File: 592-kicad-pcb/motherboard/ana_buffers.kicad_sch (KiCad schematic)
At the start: 9 parts, among them J2 U.FL, J3 U.FL, U4 OPA2328DR, U5 74LVC1T45GW

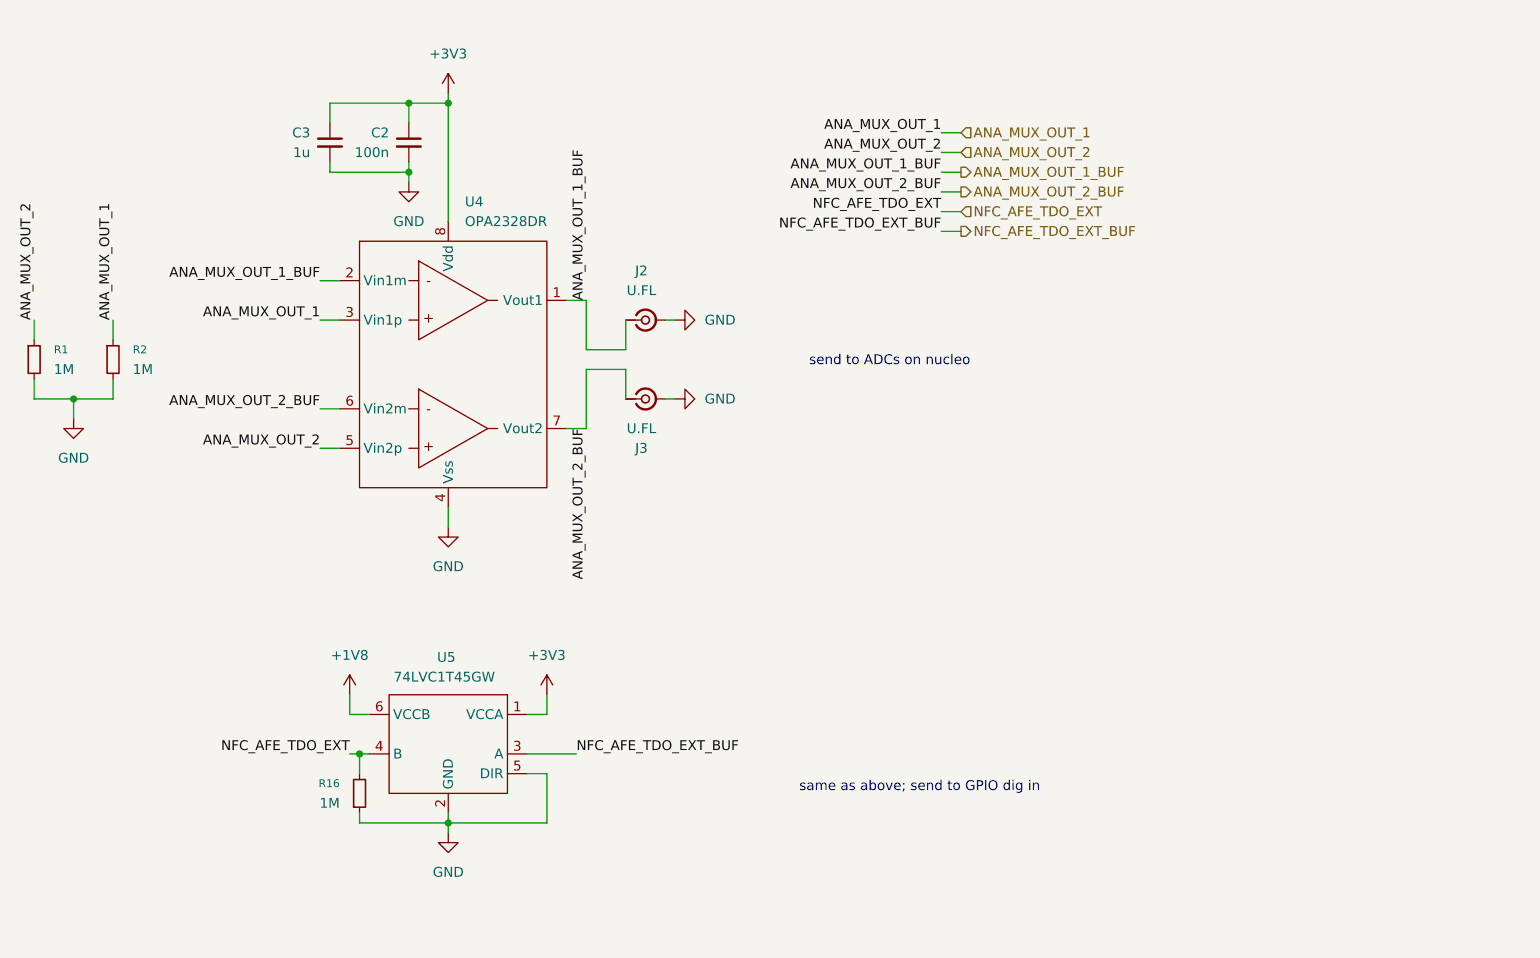
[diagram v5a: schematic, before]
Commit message: clean up schematics, add proper connectors
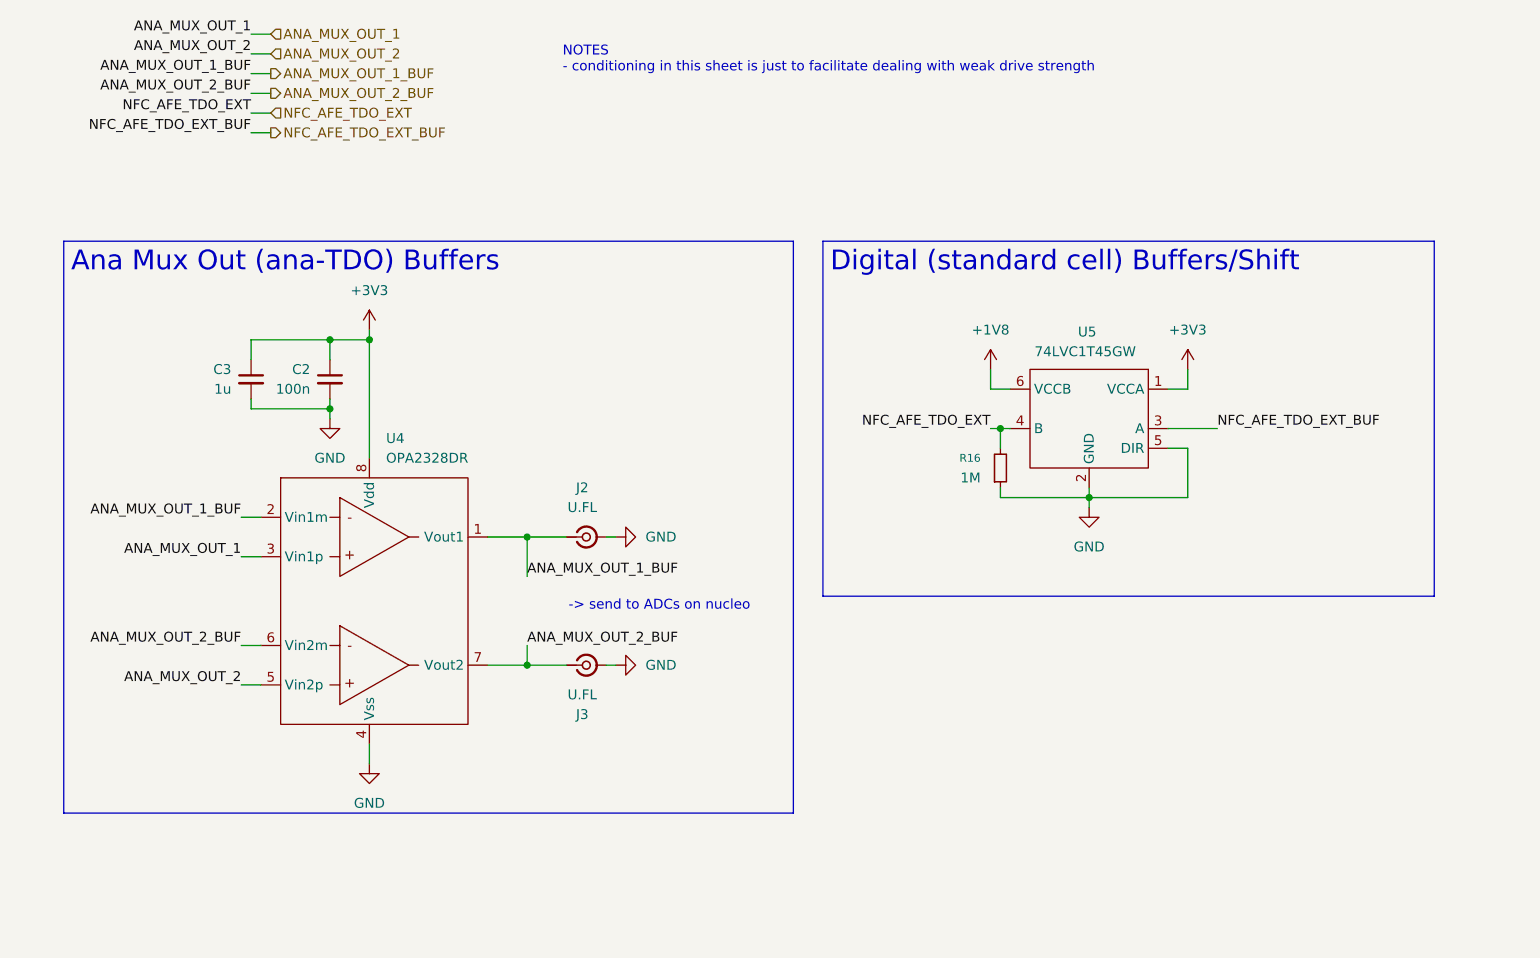
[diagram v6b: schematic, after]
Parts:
- removed R1, R2: 1M, Resistor_SMD:R_0603_1608Metric, symbol Device:R_Small
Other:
- note added: "-> send to ADCs on nucleo"
- note added: "NOTES - conditioning in this sheet is just to facilitate dealing with weak drive strength"
- note removed: "same as above; send to GPIO dig in"
- note removed: "send to ADCs on nucleo"
- moved on the sheet: C2, C3, J2, J3, R16, U4, U5

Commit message: combine hierarchy of all sans power
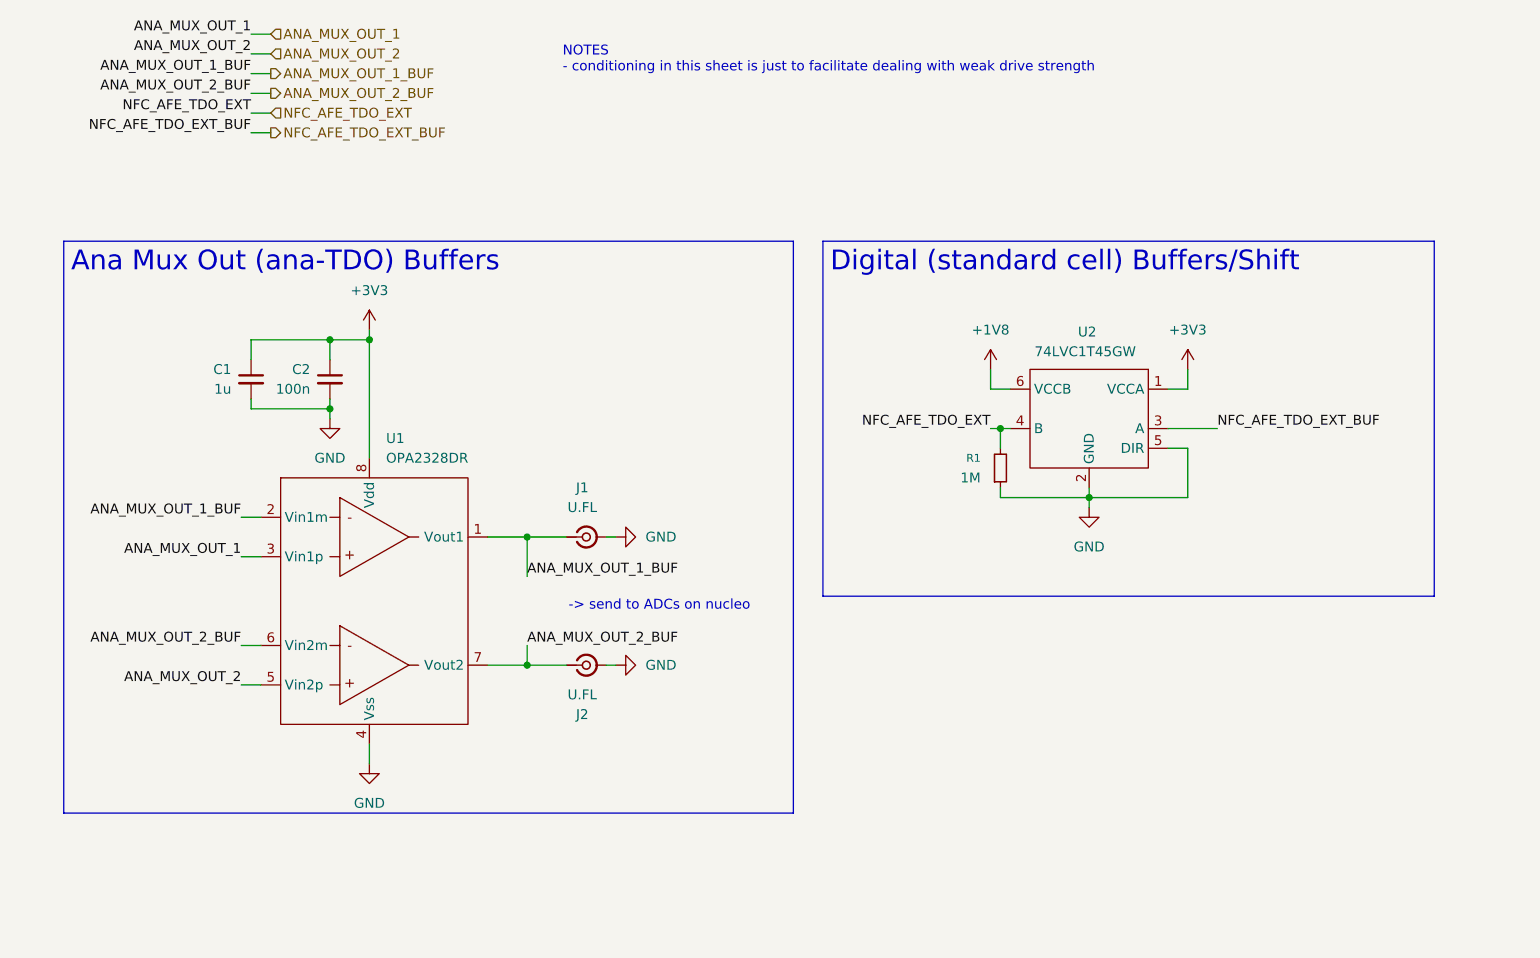
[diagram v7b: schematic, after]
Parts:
- renumbered C3 to C1, J2 to J1, J3 to J2, R16 to R1, U4 to U1, U5 to U2
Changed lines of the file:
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@@
 		(dnp no)
 		(fields_autoplaced yes)
-		(property "Reference" "#PWR019"
+		(property "Reference" "#PWR05"
 			(at 97.79 102.87 0)
 			(effects
@@
 		(instances
 			(project "motherboard"
-				(path "/5b0c97ac-fa03-4db8-b41b-0eee32b6f55d/9cc7bda2-6b63-4506-9986-d8a2a58c5915"
-					(reference "#PWR019")
+				(path "/5b0c97ac-fa03-4db8-b41b-0eee32b6f55d/f049e4ad-bebe-4338-850a-2727de737ae9/cc4799d4-5517-451a-9b97-5b1497b0c7e9"
+					(reference "#PWR05")
 					(unit 1)
 				)
@@
 		(dnp no)
 		(fields_autoplaced yes)
-		(property "Reference" "J2"
+		(property "Reference" "J1"
 			(at 87.1104 80.01 0)
 			(effects
@@
 		)
 		(instances
-			(project ""
-				(path "/5b0c97ac-fa03-4db8-b41b-0eee32b6f55d/9cc7bda2-6b63-4506-9986-d8a2a58c5915"
-					(reference "J2")
+			(project "motherboard"
+				(path "/5b0c97ac-fa03-4db8-b41b-0eee32b6f55d/f049e4ad-bebe-4338-850a-2727de737ae9/cc4799d4-5517-451a-9b97-5b1497b0c7e9"
+					(reference "J1")
 					(unit 1)
 				)
@@
 		(dnp no)
 		(fields_autoplaced yes)
-		(property "Reference" "#PWR013"
+		(property "Reference" "#PWR02"
 			(at 59.69 63.5 0)
 			(effects
@@
 		)
 		(instances
-			(project ""
-				(path "/5b0c97ac-fa03-4db8-b41b-0eee32b6f55d/9cc7bda2-6b63-4506-9986-d8a2a58c5915"
-					(reference "#PWR013")
+			(project "motherboard"
+				(path "/5b0c97ac-fa03-4db8-b41b-0eee32b6f55d/f049e4ad-bebe-4338-850a-2727de737ae9/cc4799d4-5517-451a-9b97-5b1497b0c7e9"
+					(reference "#PWR02")
 					(unit 1)
 				)
@@
 		(dnp no)
 		(fields_autoplaced yes)
-		(property "Reference" "#PWR020"
+		(property "Reference" "#PWR07"
 			(at 152.4 88.9 0)
 			(effects
@@
 		(instances
 			(project "motherboard"
-				(path "/5b0c97ac-fa03-4db8-b41b-0eee32b6f55d/9cc7bda2-6b63-4506-9986-d8a2a58c5915"
-					(reference "#PWR020")
+				(path "/5b0c97ac-fa03-4db8-b41b-0eee32b6f55d/f049e4ad-bebe-4338-850a-2727de737ae9/cc4799d4-5517-451a-9b97-5b1497b0c7e9"
+					(reference "#PWR07")
 					(unit 1)
 				)
@@
 		(dnp no)
 		(fields_autoplaced yes)
-		(property "Reference" "#PWR012"
+		(property "Reference" "#PWR03"
 			(at 59.69 121.92 0)
 			(effects
@@
 		)
 		(instances
-			(project ""
-				(path "/5b0c97ac-fa03-4db8-b41b-0eee32b6f55d/9cc7bda2-6b63-4506-9986-d8a2a58c5915"
-					(reference "#PWR012")
+			(project "motherboard"
+				(path "/5b0c97ac-fa03-4db8-b41b-0eee32b6f55d/f049e4ad-bebe-4338-850a-2727de737ae9/cc4799d4-5517-451a-9b97-5b1497b0c7e9"
+					(reference "#PWR03")
 					(unit 1)
 				)
@@
 		(on_board yes)
 		(dnp no)
-		(property "Reference" "U5"
+		(property "Reference" "U2"
 			(at 152.146 59.944 0)
 			(effects
@@
 		)
 		(instances
-			(project ""
-				(path "/5b0c97ac-fa03-4db8-b41b-0eee32b6f55d/9cc7bda2-6b63-4506-9986-d8a2a58c5915"
-					(reference "U5")
+			(project "motherboard"
+				(path "/5b0c97ac-fa03-4db8-b41b-0eee32b6f55d/f049e4ad-bebe-4338-850a-2727de737ae9/cc4799d4-5517-451a-9b97-5b1497b0c7e9"
+					(reference "U2")
 					(unit 1)
 				)
@@
 		(dnp no)
 		(fields_autoplaced yes)
-		(property "Reference" "#PWR022"
+		(property "Reference" "#PWR08"
 			(at 165.1 68.58 0)
 			(effects
@@
 		(instances
 			(project "motherboard"
-				(path "/5b0c97ac-fa03-4db8-b41b-0eee32b6f55d/9cc7bda2-6b63-4506-9986-d8a2a58c5915"
-					(reference "#PWR022")
+				(path "/5b0c97ac-fa03-4db8-b41b-0eee32b6f55d/f049e4ad-bebe-4338-850a-2727de737ae9/cc4799d4-5517-451a-9b97-5b1497b0c7e9"
+					(reference "#PWR08")
 					(unit 1)
 				)
@@
 		(dnp no)
 		(fields_autoplaced yes)
-		(property "Reference" "#PWR018"
+		(property "Reference" "#PWR04"
 			(at 97.79 86.36 0)
 			(effects
@@
 		(instances
 			(project "motherboard"
-				(path "/5b0c97ac-fa03-4db8-b41b-0eee32b6f55d/9cc7bda2-6b63-4506-9986-d8a2a58c5915"
-					(reference "#PWR018")
+				(path "/5b0c97ac-fa03-4db8-b41b-0eee32b6f55d/f049e4ad-bebe-4338-850a-2727de737ae9/cc4799d4-5517-451a-9b97-5b1497b0c7e9"
+					(reference "#PWR04")
 					(unit 1)
 				)
@@
 		(on_board yes)
 		(dnp no)
-		(property "Reference" "U4"
+		(property "Reference" "U1"
 			(at 61.8333 73.66 0)
 			(effects
@@
 		)
 		(instances
-			(project ""
-				(path "/5b0c97ac-fa03-4db8-b41b-0eee32b6f55d/9cc7bda2-6b63-4506-9986-d8a2a58c5915"
-					(reference "U4")
+			(project "motherboard"
+				(path "/5b0c97ac-fa03-4db8-b41b-0eee32b6f55d/f049e4ad-bebe-4338-850a-2727de737ae9/cc4799d4-5517-451a-9b97-5b1497b0c7e9"
+					(reference "U1")
 					(unit 1)
 				)
@@
 		(dnp no)
 		(fields_autoplaced yes)
-		(property "Reference" "#PWR014"
+		(property "Reference" "#PWR01"
 			(at 54.61 77.47 0)
 			(effects
@@
 		(instances
 			(project "motherboard"
-				(path "/5b0c97ac-fa03-4db8-b41b-0eee32b6f55d/9cc7bda2-6b63-4506-9986-d8a2a58c5915"
-					(reference "#PWR014")
+				(path "/5b0c97ac-fa03-4db8-b41b-0eee32b6f55d/f049e4ad-bebe-4338-850a-2727de737ae9/cc4799d4-5517-451a-9b97-5b1497b0c7e9"
+					(reference "#PWR01")
 					(unit 1)
 				)
@@
 		(on_board yes)
 		(dnp no)
-		(property "Reference" "J3"
+		(property "Reference" "J2"
 			(at 87.1104 109.22 0)
 			(effects
@@
 		(instances
 			(project "motherboard"
-				(path "/5b0c97ac-fa03-4db8-b41b-0eee32b6f55d/9cc7bda2-6b63-4506-9986-d8a2a58c5915"
-					(reference "J3")
+				(path "/5b0c97ac-fa03-4db8-b41b-0eee32b6f55d/f049e4ad-bebe-4338-850a-2727de737ae9/cc4799d4-5517-451a-9b97-5b1497b0c7e9"
+					(reference "J2")
 					(unit 1)
 				)
@@
 		(on_board yes)
 		(dnp no)
-		(property "Reference" "R16"
+		(property "Reference" "R1"
 			(at 138.43 76.1999 0)
 			(effects
@@
 		(instances
 			(project "motherboard"
-				(path "/5b0c97ac-fa03-4db8-b41b-0eee32b6f55d/9cc7bda2-6b63-4506-9986-d8a2a58c5915"
-					(reference "R16")
+				(path "/5b0c97ac-fa03-4db8-b41b-0eee32b6f55d/f049e4ad-bebe-4338-850a-2727de737ae9/cc4799d4-5517-451a-9b97-5b1497b0c7e9"
+					(reference "R1")
 					(unit 1)
 				)
@@
 		(on_board yes)
 		(dnp no)
-		(property "Reference" "C3"
+		(property "Reference" "C1"
 			(at 41.91 64.7762 0)
 			(effects
@@
 		(instances
 			(project "motherboard"
-				(path "/5b0c97ac-fa03-4db8-b41b-0eee32b6f55d/9cc7bda2-6b63-4506-9986-d8a2a58c5915"
-					(reference "C3")
+				(path "/5b0c97ac-fa03-4db8-b41b-0eee32b6f55d/f049e4ad-bebe-4338-850a-2727de737ae9/cc4799d4-5517-451a-9b97-5b1497b0c7e9"
+					(reference "C1")
 					(unit 1)
 				)
@@
 		)
 		(instances
-			(project ""
-				(path "/5b0c97ac-fa03-4db8-b41b-0eee32b6f55d/9cc7bda2-6b63-4506-9986-d8a2a58c5915"
+			(project "motherboard"
+				(path "/5b0c97ac-fa03-4db8-b41b-0eee32b6f55d/f049e4ad-bebe-4338-850a-2727de737ae9/cc4799d4-5517-451a-9b97-5b1497b0c7e9"
 					(reference "C2")
 					(unit 1)
@@
 		(dnp no)
 		(fields_autoplaced yes)
-		(property "Reference" "#PWR021"
+		(property "Reference" "#PWR06"
 			(at 139.7 68.58 0)
 			(effects
@@
 		)
 		(instances
-			(project ""
-				(path "/5b0c97ac-fa03-4db8-b41b-0eee32b6f55d/9cc7bda2-6b63-4506-9986-d8a2a58c5915"
-					(reference "#PWR021")
-					(unit 1)
-				)
+			(project "motherboard"
+				(path "/5b0c97ac-fa03-4db8-b41b-0eee32b6f55d/f049e4ad-bebe-4338-850a-2727de737ae9/cc4799d4-5517-451a-9b97-5b1497b0c7e9"
+					(reference "#PWR06")
+					(unit 1)
+				)

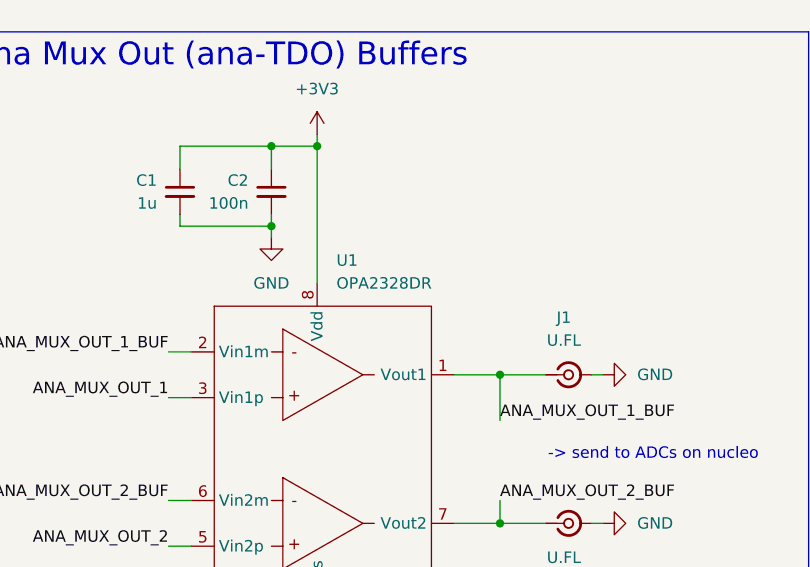
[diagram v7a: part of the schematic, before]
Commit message: add JLC part num for parts, footprints
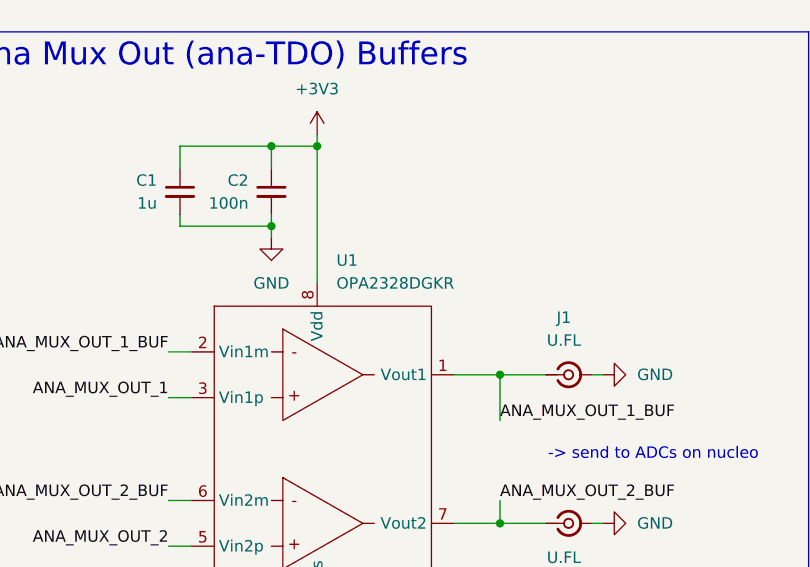
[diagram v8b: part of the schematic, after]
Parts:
- C1: LCSC (none) -> C15849
- C2: footprint Capacitor_SMD:C_0603_1608Metric -> Capacitor_SMD:C_0402_1005Metric; LCSC (none) -> C1525
- J1, J2: LCSC (none) -> C5137195
- R1: footprint Resistor_SMD:R_0603_1608Metric -> Resistor_SMD:R_0402_1005Metric; LCSC (none) -> C26083
- U1: value OPA2328DR -> OPA2328DGKR; LCSC (none) -> C5214797
- U2: LCSC (none) -> C478004
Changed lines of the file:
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@@
+			)
+		)
+		(property "LCSC" "C5137195"
+			(at 87.63 86.36 0)
+			(effects
+				(font
+					(size 1.27 1.27)
+				)
+				(hide yes)
 			)
 		)
@@
 			)
 		)
+		(property "LCSC" "C478004"
+			(at 152.4 71.12 0)
+			(effects
+				(font
+					(size 1.27 1.27)
+				)
+				(hide yes)
+			)
+		)
 		(pin "4"
 		)
@@
 			)
 		)
-		(property "Value" "OPA2328DR"
+		(property "Value" "OPA2328DGKR"
 			(at 61.8333 76.2 0)
 			(effects
@@
 		)
 		(property "Description" ""
+			(at 59.69 95.25 0)
+			(effects
+				(font
+					(size 1.27 1.27)
+				)
+				(hide yes)
+			)
+		)
+		(property "LCSC" "C5214797"
 			(at 59.69 95.25 0)
 			(effects
@@
 			)
 		)
+		(property "LCSC" "C5137195"
+			(at 87.63 102.87 0)
+			(effects
+				(font
+					(size 1.27 1.27)
+				)
+				(hide yes)
+			)
+		)
 		(pin "2"
 		)
@@
 			)
 		)
-		(property "Footprint" "Resistor_SMD:R_0603_1608Metric"
+		(property "Footprint" "Resistor_SMD:R_0402_1005Metric"
 			(at 140.97 77.47 0)
 			(effects
@@
 		)
 		(property "Description" "Resistor, small symbol"
+			(at 140.97 77.47 0)
+			(effects
+				(font
+					(size 1.27 1.27)
+				)
+				(hide yes)
+			)
+		)
+		(property "LCSC" "C26083"
 			(at 140.97 77.47 0)
 			(effects
@@
 			)
 		)
+		(property "LCSC" "C15849"
+			(at 44.45 66.04 0)
+			(effects
+				(font
+					(size 1.27 1.27)
+				)
+				(hide yes)
+			)
+		)
 		(pin "1"
 		)
@@
 			)
 		)
-		(property "Footprint" "Capacitor_SMD:C_0603_1608Metric"
+		(property "Footprint" "Capacitor_SMD:C_0402_1005Metric"
 			(at 54.61 66.04 0)
 			(effects
@@
 			(at 54.61 66.04 0)
 			(effects
+				(font
+					(size 1.27 1.27)
+				)
+				(hide yes)
+			)
+		)
+		(property "LCSC" "C1525"
+			(at 54.61 66.04 0)
+			(effects
